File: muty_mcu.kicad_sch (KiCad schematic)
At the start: 34 parts, among them J1 Conn_ARM_SWD_TagConnect_TC2030, U1 STM32F439ZITx, Y1 NX3215SA-32.768KHZ-EXS00A-MU0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, Y2 ECS-2520MVQ-160-CN-TR

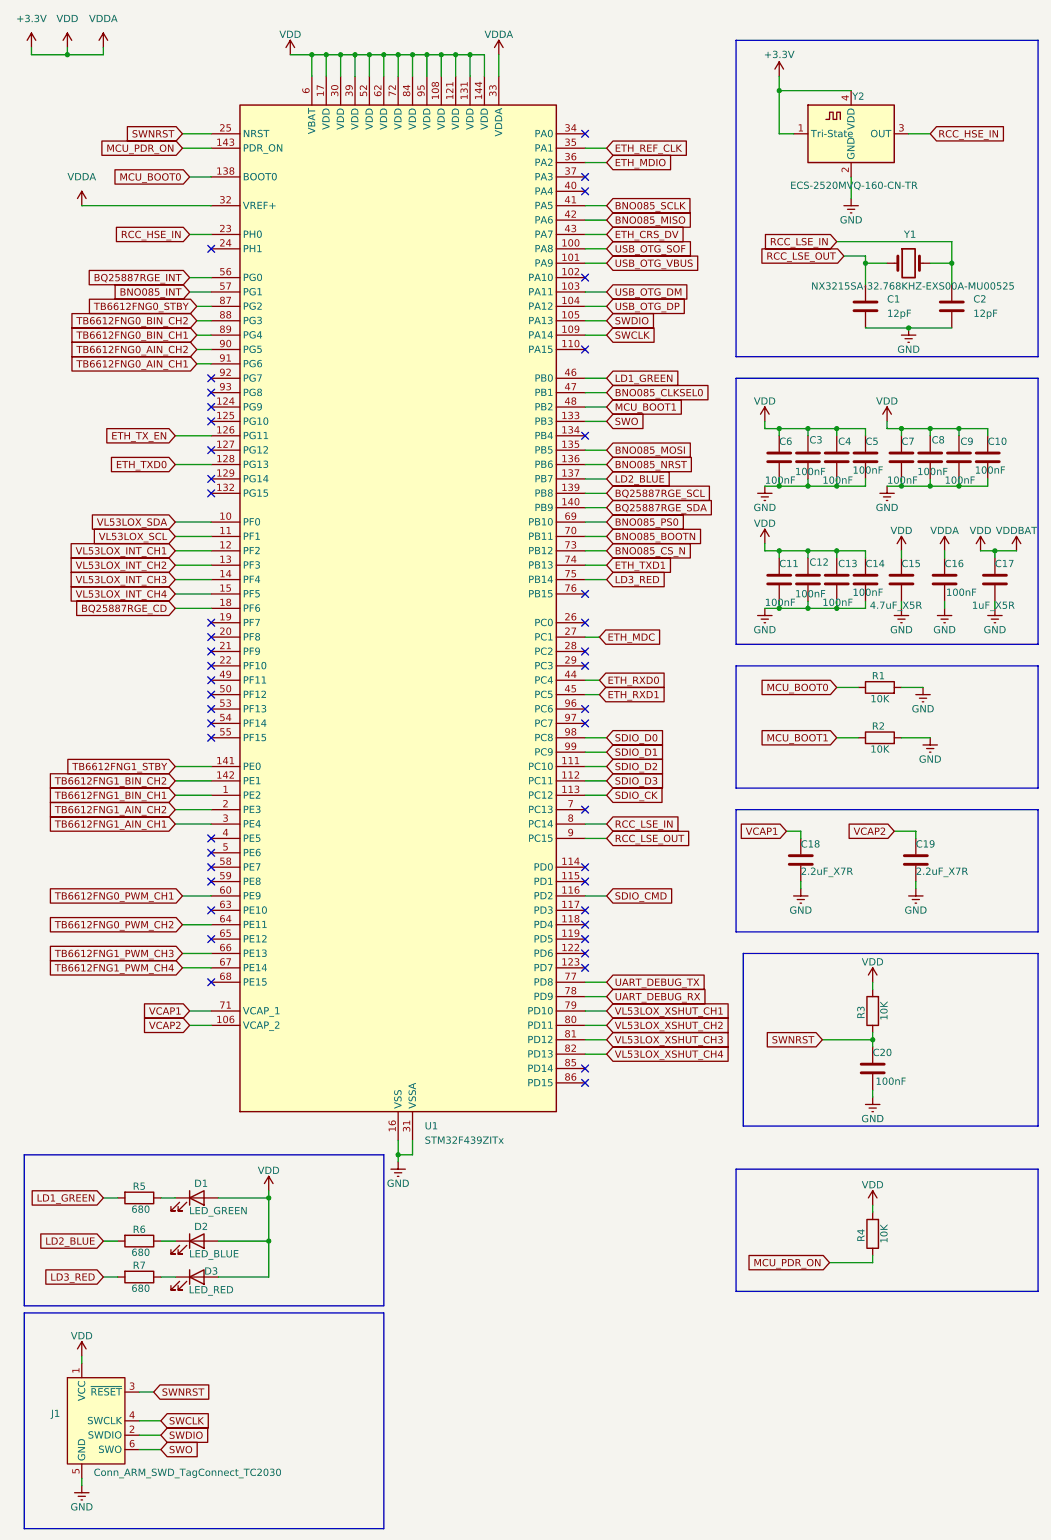
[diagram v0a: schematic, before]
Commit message: feat: add bq25887 connector
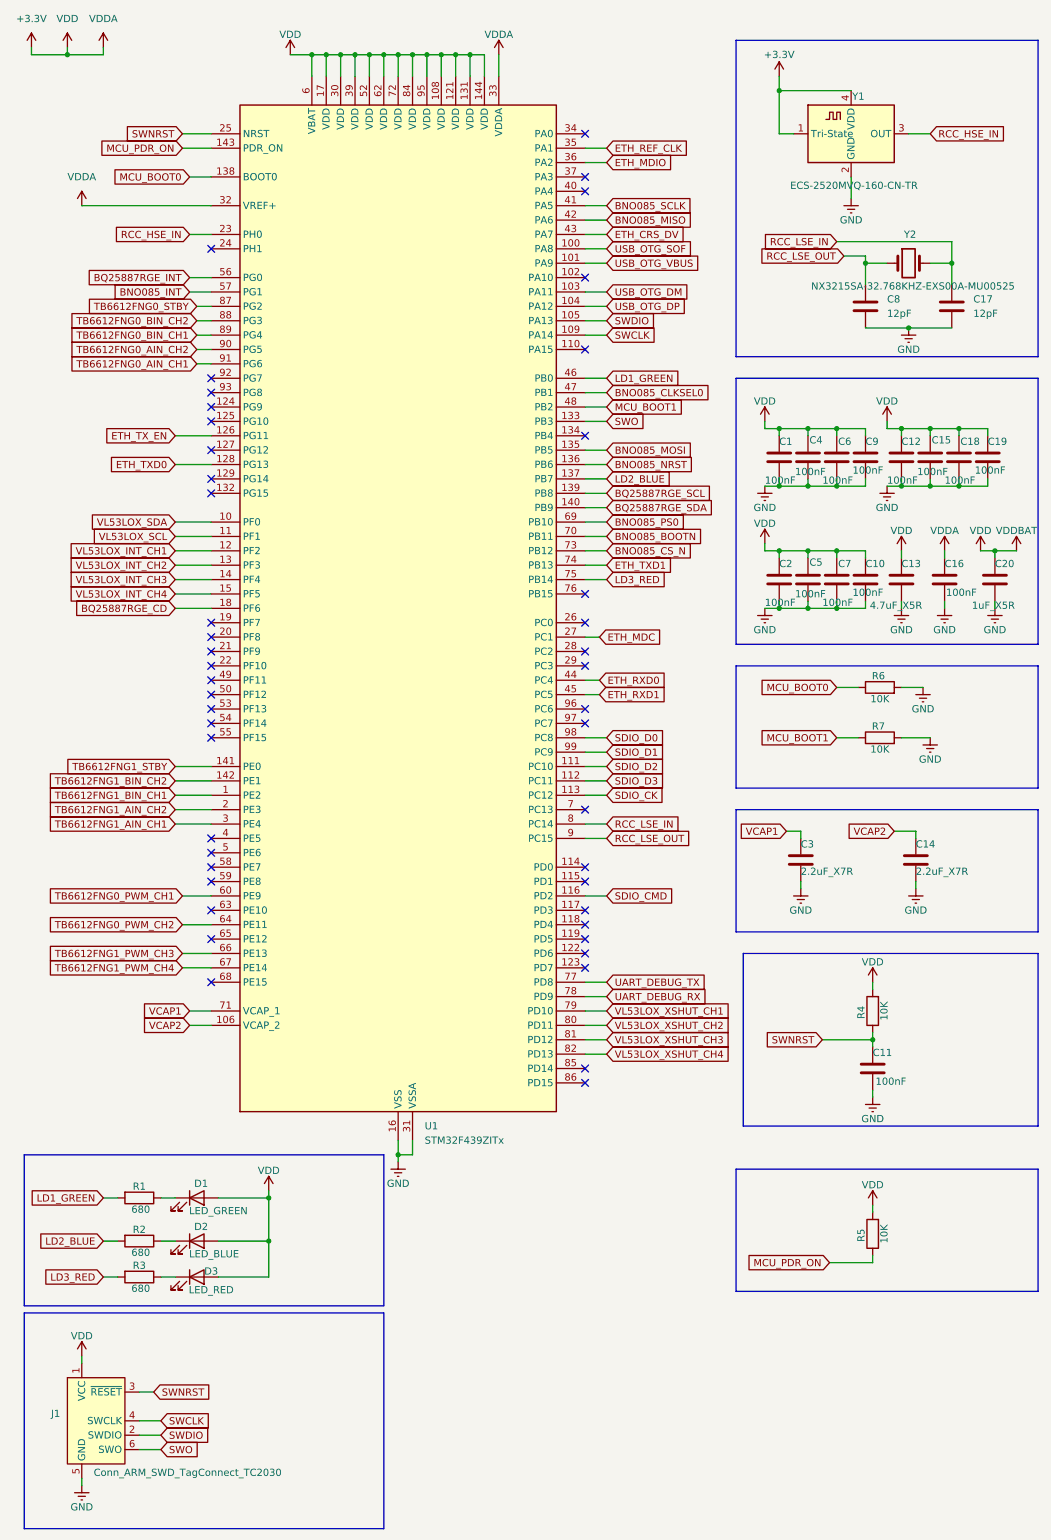
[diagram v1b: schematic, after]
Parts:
- renumbered C6 to C1, C14 to C10, C20 to C11, C7 to C12, C15 to C13, C19 to C14, C8 to C15, C2 to C17, C9 to C18, C10 to C19, C11 to C2, C17 to C20, C18 to C3, C3 to C4, C12 to C5, C4 to C6, C13 to C7, C1 to C8, C5 to C9, R5 to R1, R6 to R2, R7 to R3, R3 to R4, R4 to R5, R1 to R6, R2 to R7, Y2 to Y1, Y1 to Y2
